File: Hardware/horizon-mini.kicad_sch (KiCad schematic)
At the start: 78 parts, among them J16 arming terminal, J2 Conn_01x02_Pin, J3 Micro_SD_Card_Det1, J4 Screw_Terminal_01x02, J7 USB_C_Receptacle_USB2.0_16P, J8 Conn_02x03_Counter_Clockwise, Q1 BSS138, Q10 DMG2301L, Q2 AO3400A, U1 TPS82130, U16 AP2112K-3.3, U2 TPS61092, U3 LTC4412xS6, U4 BMP581, U5 ATSAMD21G18A-A, U6 NAND, U7 INA219BxD, U9 LSM6DS3

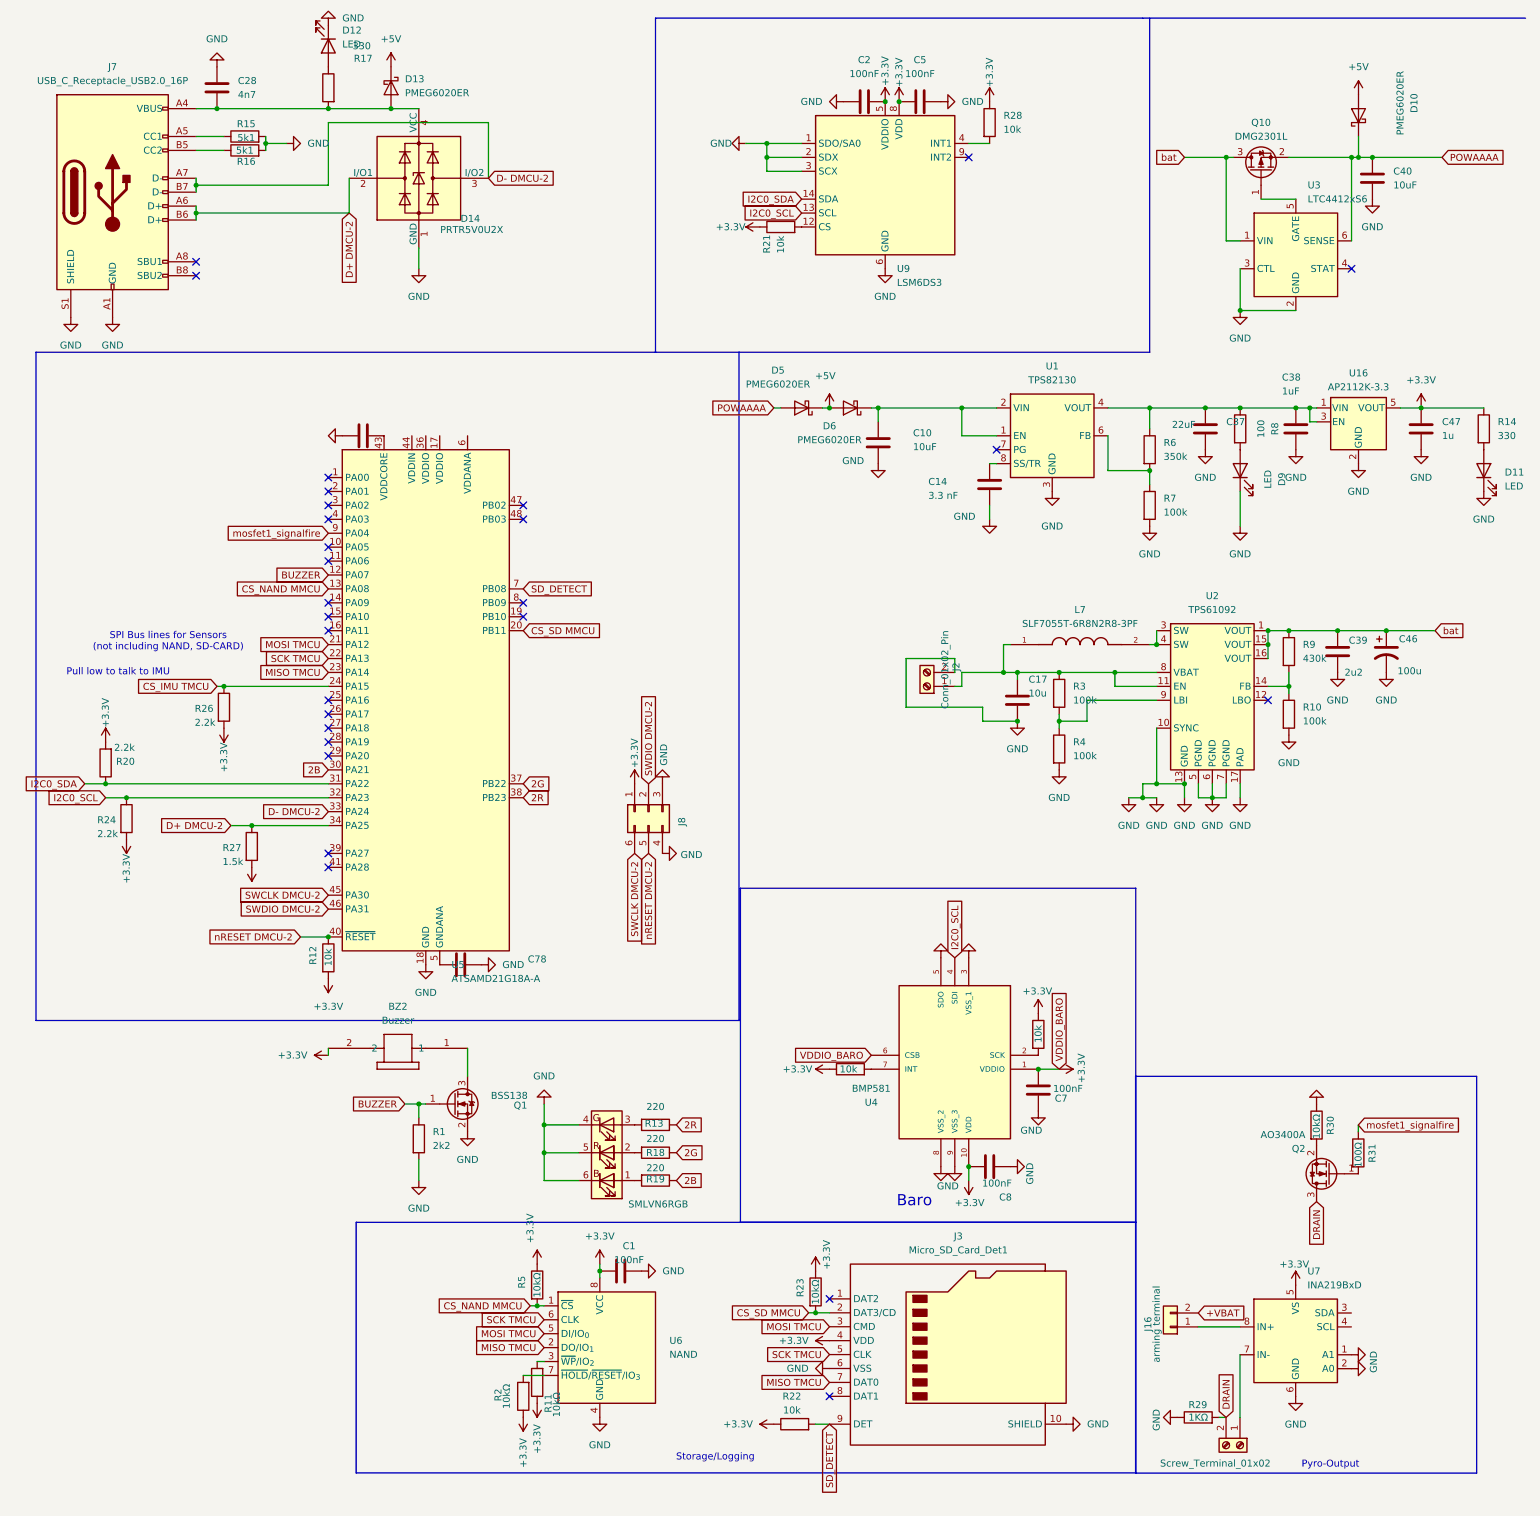
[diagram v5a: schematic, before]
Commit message: ah yes, I love that I forgot to push lol. Fixed pyro + rerouted to save space.
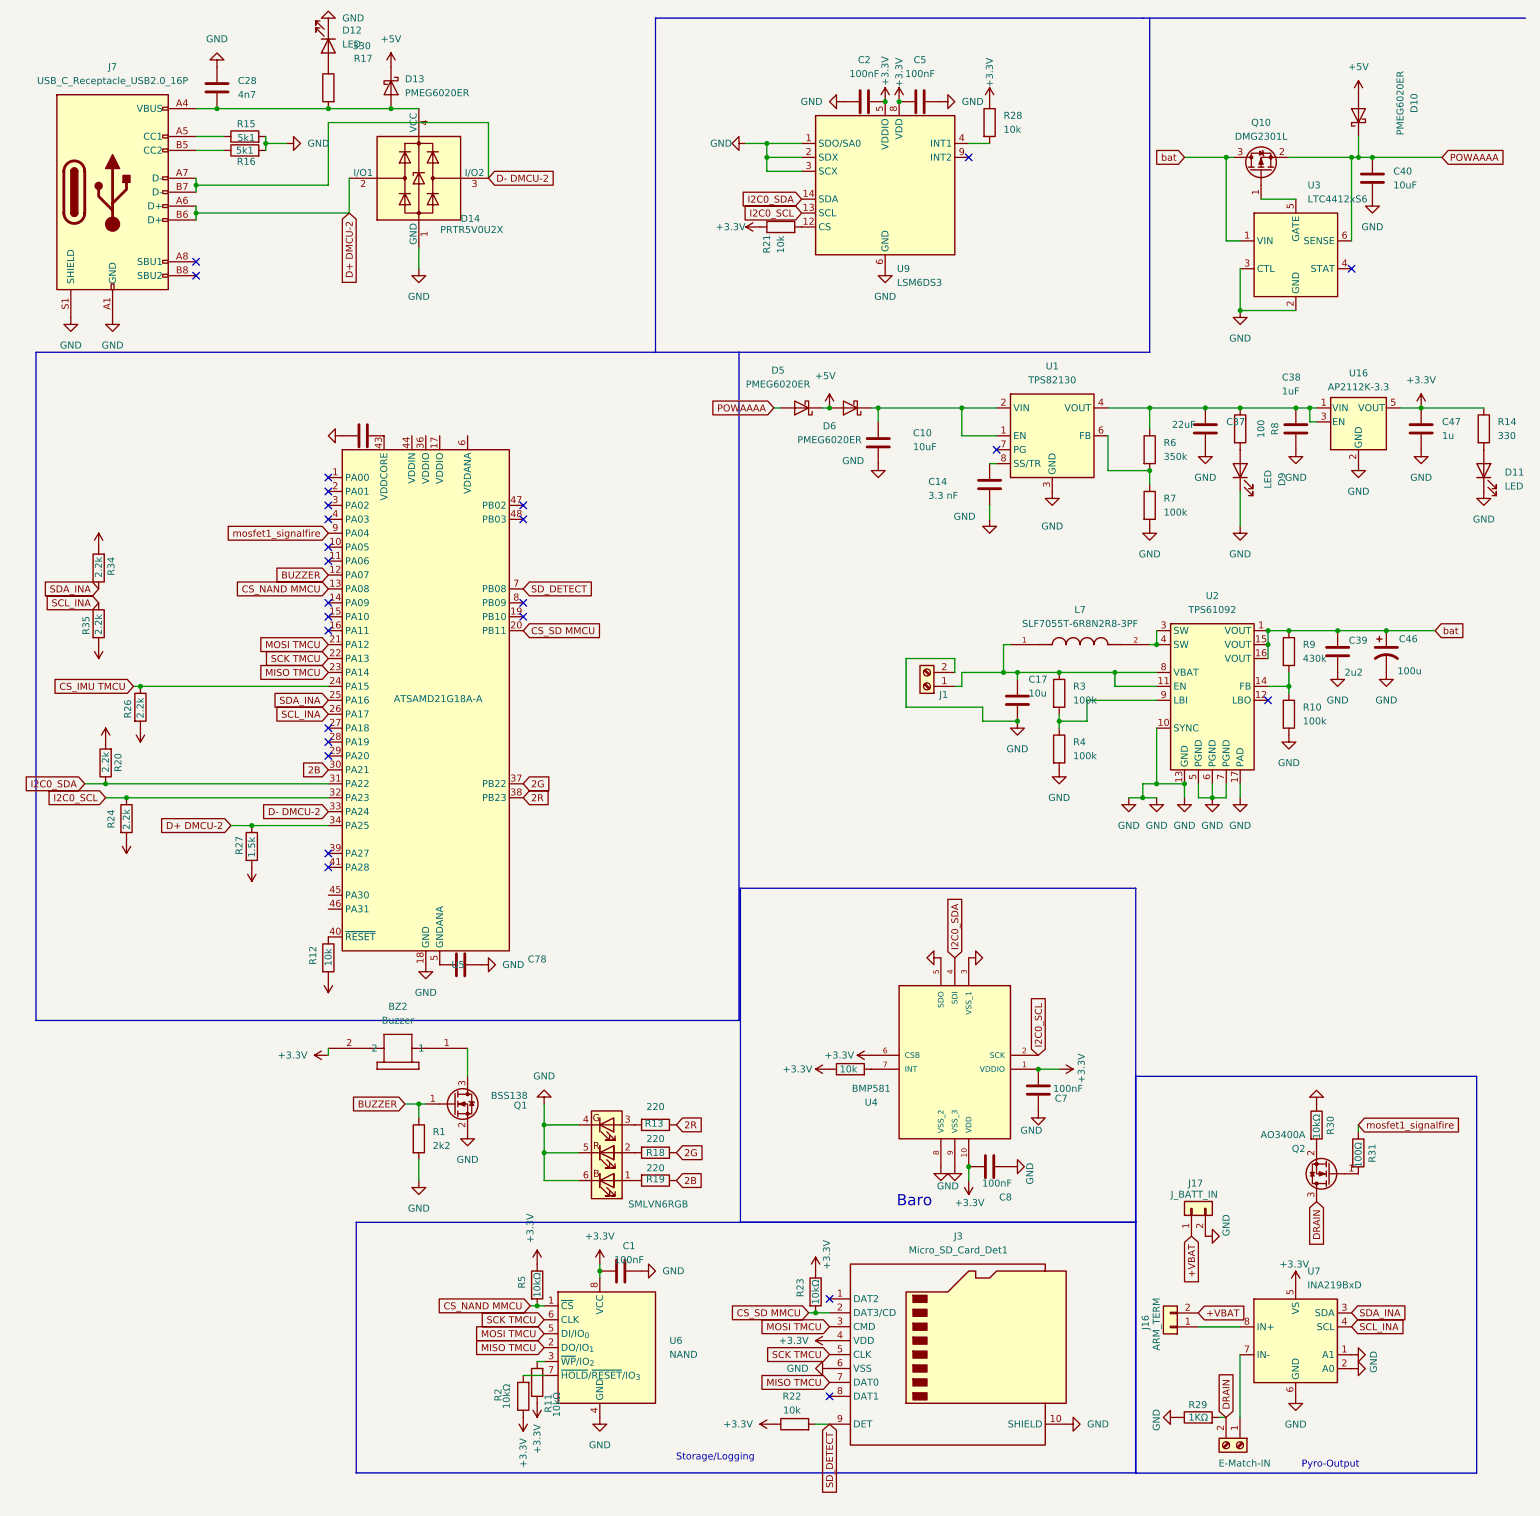
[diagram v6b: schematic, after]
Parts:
- removed J2: Conn_01x02_Pin, Connector_JST:JST_PH_B2B-PH-K_1x02_P2.00mm_Vertical, symbol Connector:Screw_Terminal_01x02
- removed J8: Conn_02x03_Counter_Clockwise, Connector_PinHeader_2.54mm:PinHeader_2x03_P2.54mm_Vertical, symbol Connector_Generic:Conn_02x03_Counter_Clockwise
- removed R32: 10k, Resistor_SMD:R_0603_1608Metric, symbol Device:R
- added J1: Screw_Terminal_01x02, TerminalBlock_Phoenix:TerminalBlock_Phoenix_MPT-0,5-2-2.54_1x02_P2.54mm_Horizontal, symbol Connector:Screw_Terminal_01x02
- added J17: J_BATT_IN, Connector_PinHeader_1.27mm:PinHeader_1x02_P1.27mm_Vertical, symbol Connector_Generic:Conn_01x02
- added R34, R35: 2.2k, Resistor_SMD:R_0402_1005Metric, symbol Device:R
- C1, C10, C14, C17, C2, C28, C37, C38, C39, C40, C46, C47, C5, C6, C78: footprint Capacitor_SMD:C_0603_1608Metric -> Capacitor_SMD:C_0402_1005Metric
- C7, C8: footprint (none) -> Capacitor_SMD:C_0402_1005Metric
- J16: value arming terminal -> ARM_TERM; footprint TerminalBlock_Phoenix:TerminalBlock_Phoenix_MPT-0,5-2-2.54_1x02_P2.54mm_Horizontal -> Connector_PinHeader_1.27mm:PinHeader_1x02_P1.27mm_Vertical
- J4: value Screw_Terminal_01x02 -> E-Match-IN
- R1, R10, R11, R12, R13, R14, R15, R16, R17, R18, R19, R2, R20, R21, R22, R23, R24, R26, R27, R28, R3, R33, R4, R5, R6, R7, R8, R9: footprint Resistor_SMD:R_0603_1608Metric -> Resistor_SMD:R_0402_1005Metric
- R29, R30, R31: footprint (none) -> Resistor_SMD:R_0402_1005Metric
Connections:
- net +3.3V: now also R34.2, R35.2
- net +VBAT: now also J17.1 (Pin_1)
- net GND: now also J1.2 (Pin_2), J17.2 (Pin_2)
- net I2C0_SCL: now also U4.2 (SCK); no longer U4.4 (SDI)
- net I2C0_SDA: now also U4.4 (SDI)
- net SDA_INA: now reaches U5.25 (PA16)
- net SDA_INA: now also R34.1
- net SCL_INA: now reaches U5.26 (PA17)
- net SCL_INA: now also R35.1
- net at C17.1, L7.1, R3.1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: now also J1.1 (Pin_1)
- net SWCLK DMCU-2: no longer names the net of U5.45 (PA30)
- net SWDIO DMCU-2: no longer names the net of U5.46 (PA31)
- net nRESET DMCU-2: no longer names the net of R12.1, U5.40 (~{RESET})
- no-connect marks 28 -> 26
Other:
- note removed: "Pull low to talk to IMU"
- note removed: "SPI Bus lines for Sensors (not including NAND, SD-CARD)"
- moved on the sheet: R26
